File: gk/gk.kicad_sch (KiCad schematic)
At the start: 61 parts, among them J1 USB_C_Receptacle_USB2.0, J10 Barrel_Jack_Switch, J2 Conn_01x02, J8 Conn_ARM_JTAG_SWD_10, U1 WE-TVS-82400102, U10 MAX17048, U2 MCP73831-2-OT, U3 AP62300WU

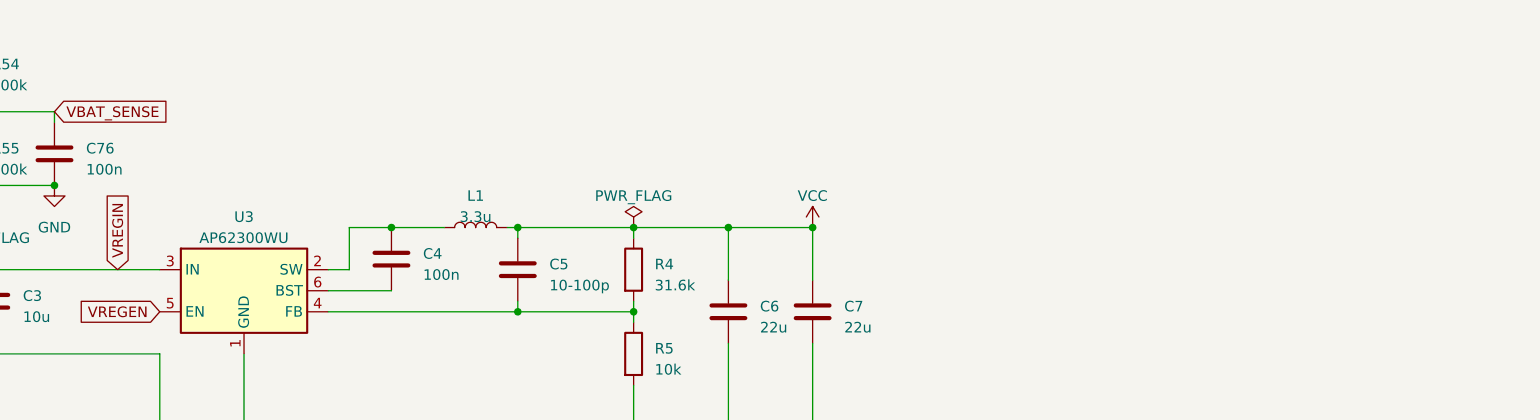
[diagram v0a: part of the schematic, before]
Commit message: add power supply TODOs to pcb
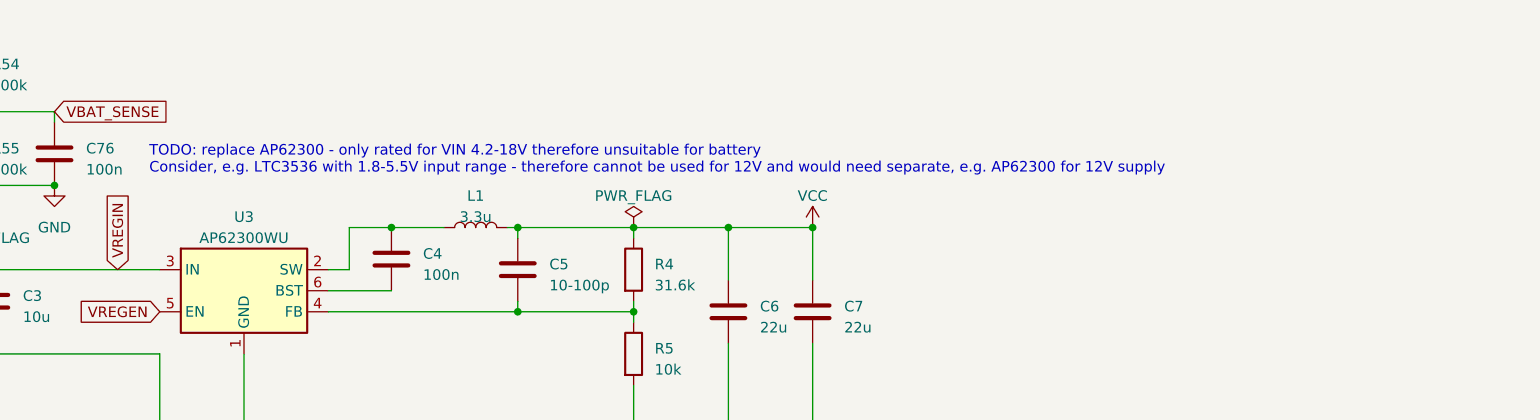
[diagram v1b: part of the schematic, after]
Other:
- note added: "TODO: replace AP62300 - only rated for VIN 4.2-18V therefore unsuitable for battery Consider, e.g. LTC3536 with 1.8-5.5V input range - therefore cannot be used for 12V and would need separate, e.g. AP62300 for 12V supply"
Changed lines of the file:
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@@
+    (effects (font (size 1.27 1.27)) (justify left bottom))
+  )
+  (text "TODO: replace AP62300 - only rated for VIN 4.2-18V therefore unsuitable for battery\nConsider, e.g. LTC3536 with 1.8-5.5V input range - therefore cannot be used for 12V and would need separate, e.g. AP62300 for 12V supply"
+    (at 187.96 34.29 0)
     (effects (font (size 1.27 1.27)) (justify left bottom))
   )
